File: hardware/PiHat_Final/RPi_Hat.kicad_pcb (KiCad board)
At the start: 2 copper layers, 65 x 56.5 mm, 5 parts, among them J2 RPi_GPIO

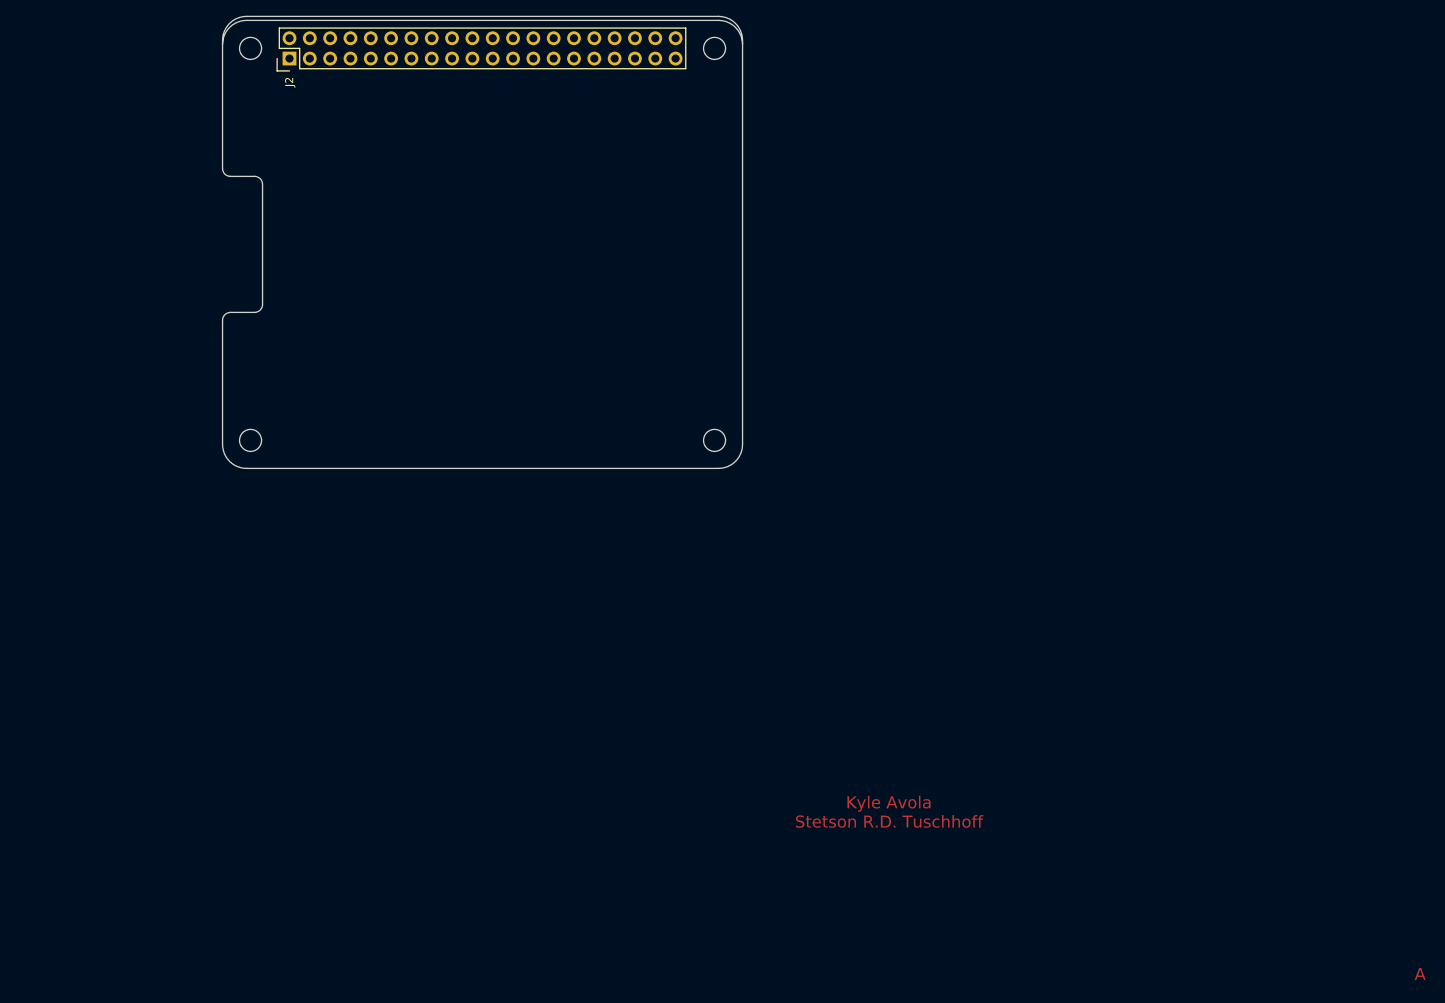
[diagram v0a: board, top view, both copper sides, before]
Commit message: Began Layout, Pihat final.
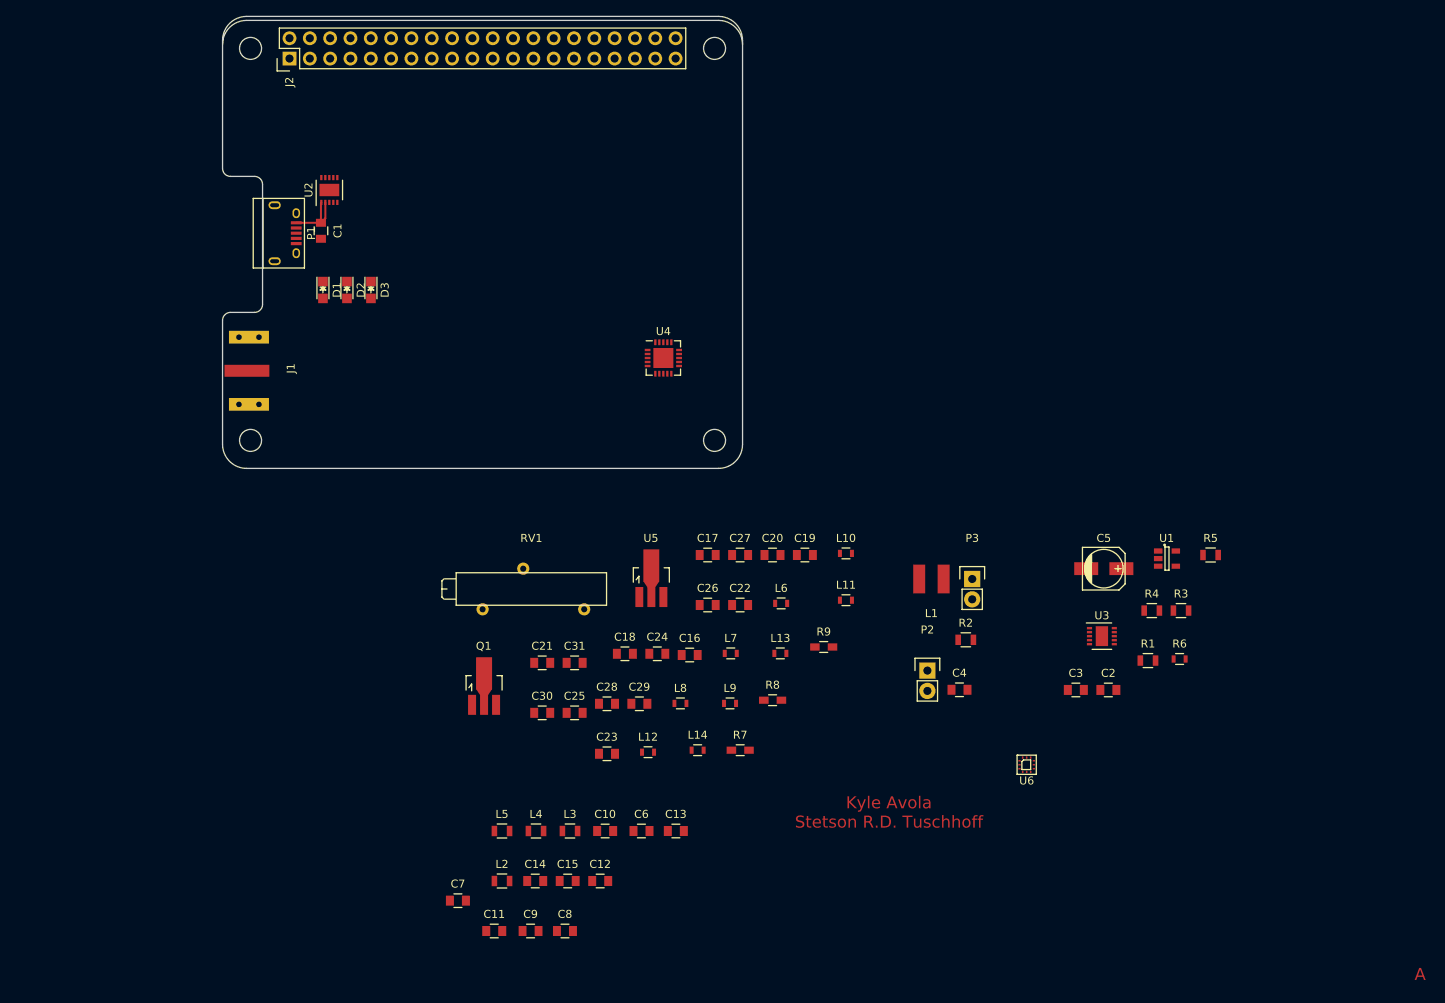
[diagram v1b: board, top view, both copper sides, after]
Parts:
- added C1: 10uF, Capacitors_SMD:C_0805, F.Cu at (131.2, 100.1)
- added C10: 5.6pF, Capacitors_SMD:C_0805, F.Cu at (166.8, 175.1)
- added C11: 4.7pF, Capacitors_SMD:C_0805, F.Cu at (152.9, 187.6)
- added C12: 10nF, Capacitors_SMD:C_0805, F.Cu at (166.2, 181.4)
- added C13: 10nF, Capacitors_SMD:C_0805, F.Cu at (175.6, 175.1)
- added C14: 20pF, Capacitors_SMD:C_0805, F.Cu at (158.0, 181.4)
- added C15: 20pF, Capacitors_SMD:C_0805, F.Cu at (162.1, 181.4)
- added C16: C, Capacitors_SMD:C_0805, F.Cu at (177.3, 153.1)
- added C17: C, Capacitors_SMD:C_0805, F.Cu at (179.6, 140.6)
- added C18: C, Capacitors_SMD:C_0805, F.Cu at (169.2, 153.0)
- added C19: C, Capacitors_SMD:C_0805, F.Cu at (191.7, 140.6)
- added C2: 10uF, Capacitors_SMD:C_0805, F.Cu at (229.7, 157.5)
- added C20: C, Capacitors_SMD:C_0805, F.Cu at (187.7, 140.6)
- added C21: C, Capacitors_SMD:C_0805, F.Cu at (158.9, 154.1)
- added C22: C, Capacitors_SMD:C_0805, F.Cu at (183.6, 146.9)
- added C23: C, Capacitors_SMD:C_0805, F.Cu at (167.0, 165.5)
- added C24: C, Capacitors_SMD:C_0805, F.Cu at (173.3, 153.0)
- added C25: C, Capacitors_SMD:C_0805, F.Cu at (163.0, 160.4)
- added C26: C, Capacitors_SMD:C_0805, F.Cu at (179.6, 146.9)
- added C27: C, Capacitors_SMD:C_0805, F.Cu at (183.6, 140.6)
- added C28: C, Capacitors_SMD:C_0805, F.Cu at (167.0, 159.2)
- added C29: C, Capacitors_SMD:C_0805, F.Cu at (171.1, 159.2)
- added C3: 10uF, Capacitors_SMD:C_0805, F.Cu at (225.6, 157.5)
- added C30: C, Capacitors_SMD:C_0805, F.Cu at (158.9, 160.4)
- added C31: C, Capacitors_SMD:C_0805, F.Cu at (163.0, 154.1)
- added C4: 10uF, Capacitors_SMD:C_0805, F.Cu at (211.1, 157.5)
- added C5: 47uF, Capacitors_SMD:c_elec_5x5.3, F.Cu at (229.1, 142.3)
- added C6: 4.7pF, Capacitors_SMD:C_0805, F.Cu at (171.3, 175.1)
- added C7: 5.1pF, Capacitors_SMD:C_0805, F.Cu at (148.4, 183.8)
- added C8: 12pF, Capacitors_SMD:C_0805, F.Cu at (161.8, 187.6)
- added C9: 4.7pF, Capacitors_SMD:C_0805, F.Cu at (157.5, 187.6)
- added D1: LED, LEDs:LED_0805, F.Cu at (131.5, 107.5)
- added D2: LED, LEDs:LED_0805, F.Cu at (134.5, 107.5)
- added D3: LED, LEDs:LED_0805, F.Cu at (137.5, 107.5)
- added J1: SMACONN, RF BW Filter:SMA_Edge_Mount, F.Cu at (122.0, 117.6)
- added L1: 6.8uH, inductor:BOURNES_SRN4018, F.Cu at (207.6, 143.6)
- added L10: L_Small, Resistors_SMD:R_0603, F.Cu at (196.9, 140.4)
- added L11: L_Small, Resistors_SMD:R_0603, F.Cu at (196.9, 146.3)
- added L12: L_Small, Resistors_SMD:R_0603, F.Cu at (172.1, 165.3)
- added L13: L_Small, Resistors_SMD:R_0603, F.Cu at (188.7, 152.9)
- added L14: L_Small, Resistors_SMD:R_0603, F.Cu at (178.3, 165.0)
- added L2: 11nH, Resistors_SMD:R_0805, F.Cu at (153.9, 181.4)
- added L3: 27nH, Resistors_SMD:R_0805, F.Cu at (162.4, 175.1)
- added L4: 36nH, Resistors_SMD:R_0805, F.Cu at (158.1, 175.1)
- added L5: 36nH, Resistors_SMD:R_0805, F.Cu at (153.9, 175.1)
- added L6: L_Small, Resistors_SMD:R_0603, F.Cu at (188.8, 146.7)
- added L7: L_Small, Resistors_SMD:R_0603, F.Cu at (182.5, 152.9)
- added L8: L_Small, Resistors_SMD:R_0603, F.Cu at (176.2, 159.2)
- added L9: L_Small, Resistors_SMD:R_0603, F.Cu at (182.4, 159.2)
- added P1: USB_OTG, Connect:USB_Micro-B, F.Cu at (126.6, 100.4)
- added P2: BATT, Pin_Headers:Pin_Header_Straight_1x02, F.Cu at (207.1, 155.1)
- added P3: THERM, Pin_Headers:Pin_Header_Straight_1x02, F.Cu at (212.7, 143.6)
- added Q1: AFT05MS003N, TO_SOT_Packages_SMD:SOT89-3_Housing_Handsoldering, F.Cu at (151.6, 157.0)
- added R1: 1K, Resistors_SMD:R_0805, F.Cu at (234.6, 153.8)
- added R2: 1K, Resistors_SMD:R_0805, F.Cu at (211.9, 151.2)
- added R3: 1K, Resistors_SMD:R_0805, F.Cu at (238.8, 147.6)
- added R4: 1K, Resistors_SMD:R_0805, F.Cu at (235.1, 147.6)
- added R5: 1K, Resistors_SMD:R_0805, F.Cu at (242.5, 140.6)
- added R6: 150K, Resistors_SMD:R_0603, F.Cu at (238.6, 153.6)
- added R7: R, Resistors_SMD:R_0603_HandSoldering, F.Cu at (183.7, 165.0)
- added R8: R, Resistors_SMD:R_0603_HandSoldering, F.Cu at (187.7, 158.8)
- added R9: R, Resistors_SMD:R_0603_HandSoldering, F.Cu at (194.1, 152.1)
- added RV1: POT, Potentiometers:Potentiometer_Bourns_3006W_Angular_ScrewFront, F.Cu at (164.2, 147.4)
- added U1: MCP3021, TO_SOT_Packages_SMD:SOT-23-5, F.Cu at (237.0, 141.1)
- added U2: MCP73833, Housings_DFN_QFN:DFN-10-1EP_3x3mm_Pitch0.5mm, F.Cu at (132.3, 95.0)
- added U3: TPS61027, Housings_DFN_QFN:DFN-10-1EP_3x3mm_Pitch0.5mm, F.Cu at (228.9, 150.8)
- added U4: Si4464, Housings_DFN_QFN:QFN-20-1EP_4x4mm_Pitch0.5mm, F.Cu at (174.1, 116.0)
- added U5: MMG3H21NT1, TO_SOT_Packages_SMD:SOT89-3_Housing_Handsoldering, F.Cu at (172.5, 143.5)
- added U6: SKY13374, RFBRD:QFN_12_2mmx2mm_0.5PITCH, F.Cu at (219.5, 166.8)
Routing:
- net 5VU: track 0.00 -> 8.44 mm

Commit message: PCB Layout Changes
minor changes, will continue layout
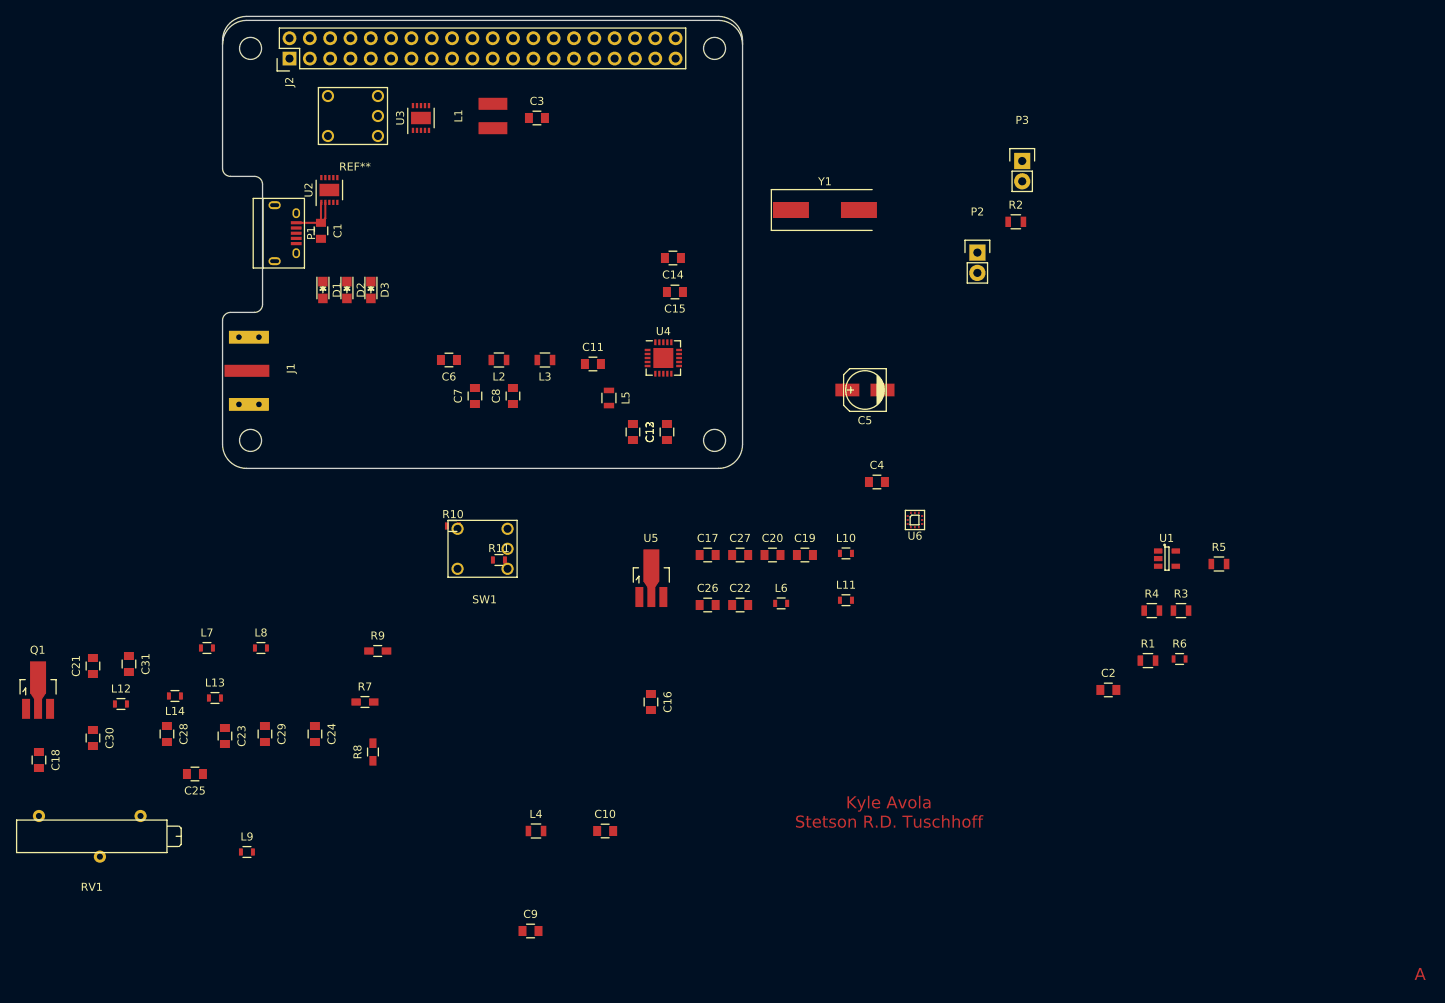
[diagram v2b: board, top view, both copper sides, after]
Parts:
- added R10: R, Resistors_SMD:R_0603, F.Cu at (147.8, 137.0)
- added R11: R, Resistors_SMD:R_0603, F.Cu at (153.5, 141.2)
- added REF**: rotary_potentiometer, rotary_potentiometer:rotary_potentiometer, F.Cu at (135.2, 85.8)
- added SW1: PWR_VOL, rotary_potentiometer:rotary_potentiometer, F.Cu at (151.4, 139.9)
- added Y1: 30MHz, Crystals:Crystal_SMD_HC49-SD, F.Cu at (194.2, 97.5)
- moved U3 107.0 mm to (143.8, 86.0), turned to 90 degrees
- moved C3 98.2 mm to (158.2, 86.0)
- moved C14 79.8 mm to (175.2, 103.5), turned to 180 degrees
- moved L1 79.7 mm to (152.8, 85.8), turned to 270 degrees
- moved C15 74.8 mm to (175.5, 107.8), turned to 180 degrees
- moved C18 74.4 mm to (96.0, 166.2), turned to 270 degrees
- moved RV1 72.9 mm to (96.0, 173.2), turned to 180 degrees
- moved C11 71.9 mm to (165.2, 116.8)
- moved L13 70.9 mm to (118.0, 158.5)
- moved C8 67.2 mm to (155.2, 120.8), turned to 90 degrees
- moved L12 66.2 mm to (106.2, 159.2)
- moved L14 65.7 mm to (113.0, 158.2), turned to 180 degrees
- moved L7 65.5 mm to (117.0, 152.2)
- moved L2 65.1 mm to (153.5, 116.2), turned to 180 degrees
- moved C6 63.6 mm to (147.2, 116.2), turned to 180 degrees
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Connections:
- J2 pad 1: (no net) -> Net-(J2-Pad1)
- J2 pad 10: (no net) -> Net-(J2-Pad10)
- J2 pad 11: (no net) -> Net-(J2-Pad11)
- J2 pad 12: (no net) -> Net-(J2-Pad12)
- J2 pad 13: (no net) -> Net-(J2-Pad13)
- J2 pad 14: (no net) -> Net-(J2-Pad14)
- J2 pad 15: (no net) -> Net-(J2-Pad15)
- J2 pad 16: (no net) -> Net-(J2-Pad16)
- J2 pad 17: (no net) -> Net-(J2-Pad17)
- J2 pad 18: (no net) -> Net-(J2-Pad18)
- J2 pad 19: (no net) -> Net-(J2-Pad19)
- J2 pad 2: (no net) -> Net-(J2-Pad2)
- J2 pad 20: (no net) -> Net-(J2-Pad20)
- J2 pad 21: (no net) -> Net-(J2-Pad21)
- J2 pad 22: (no net) -> Net-(J2-Pad22)
- J2 pad 23: (no net) -> Net-(J2-Pad23)
- J2 pad 24: (no net) -> Net-(J2-Pad24)
- J2 pad 25: (no net) -> Net-(J2-Pad25)
- J2 pad 26: (no net) -> Net-(J2-Pad26)
- J2 pad 27: (no net) -> Net-(J2-Pad27)
- J2 pad 28: (no net) -> Net-(J2-Pad28)
- J2 pad 29: (no net) -> Net-(J2-Pad29)
- J2 pad 3: (no net) -> Net-(J2-Pad3)
- J2 pad 30: (no net) -> Net-(J2-Pad30)
- J2 pad 31: (no net) -> Net-(J2-Pad31)
- J2 pad 32: (no net) -> Net-(J2-Pad32)
- J2 pad 33: (no net) -> Net-(J2-Pad33)
- J2 pad 34: (no net) -> Net-(J2-Pad34)
- J2 pad 35: (no net) -> Net-(J2-Pad35)
- J2 pad 36: (no net) -> Net-(J2-Pad36)
- J2 pad 37: (no net) -> Net-(J2-Pad37)
- J2 pad 38: (no net) -> Net-(J2-Pad38)
- J2 pad 39: (no net) -> Net-(J2-Pad39)
- J2 pad 4: (no net) -> Net-(J2-Pad4)
- J2 pad 40: (no net) -> Net-(J2-Pad40)
- J2 pad 5: (no net) -> Net-(J2-Pad5)
- J2 pad 6: (no net) -> Net-(J2-Pad6)
- J2 pad 7: (no net) -> Net-(J2-Pad7)
- J2 pad 8: (no net) -> Net-(J2-Pad8)
- J2 pad 9: (no net) -> Net-(J2-Pad9)
- P1 pad 2: (no net) -> Net-(P1-Pad2)
- P1 pad 3: (no net) -> Net-(P1-Pad3)
- P1 pad 4: (no net) -> Net-(P1-Pad4)
- U1 pad 3: (no net) -> VOL
- U1 pad 4: (no net) -> SDA
- U1 pad 5: (no net) -> SCL
- U3 pad 3: (no net) -> Net-(U3-Pad3)
- U3 pad 4: (no net) -> Net-(U3-Pad4)
- U3 pad 7: (no net) -> Net-(U3-Pad7)
- U4 pad 1: (no net) -> SHDN
- U4 pad 10: (no net) -> Net-(U4-Pad10)
- U4 pad 11: (no net) -> nIRQ
- U4 pad 12: (no net) -> SCLK
- U4 pad 13: (no net) -> SDO
- U4 pad 14: (no net) -> SDI
- U4 pad 15: (no net) -> nSEL
- U4 pad 19: (no net) -> Net-(U4-Pad19)
- U4 pad 20: (no net) -> Net-(U4-Pad20)
- U4 pad 5: (no net) -> Net-(U4-Pad5)
- U4 pad 7: (no net) -> Net-(U4-Pad7)
- U4 pad 9: (no net) -> Net-(U4-Pad9)
- U6 pad 1: (no net) -> Net-(U6-Pad1)
- U6 pad 7: (no net) -> SEL_1

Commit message: Pihat PCB Changes
layout
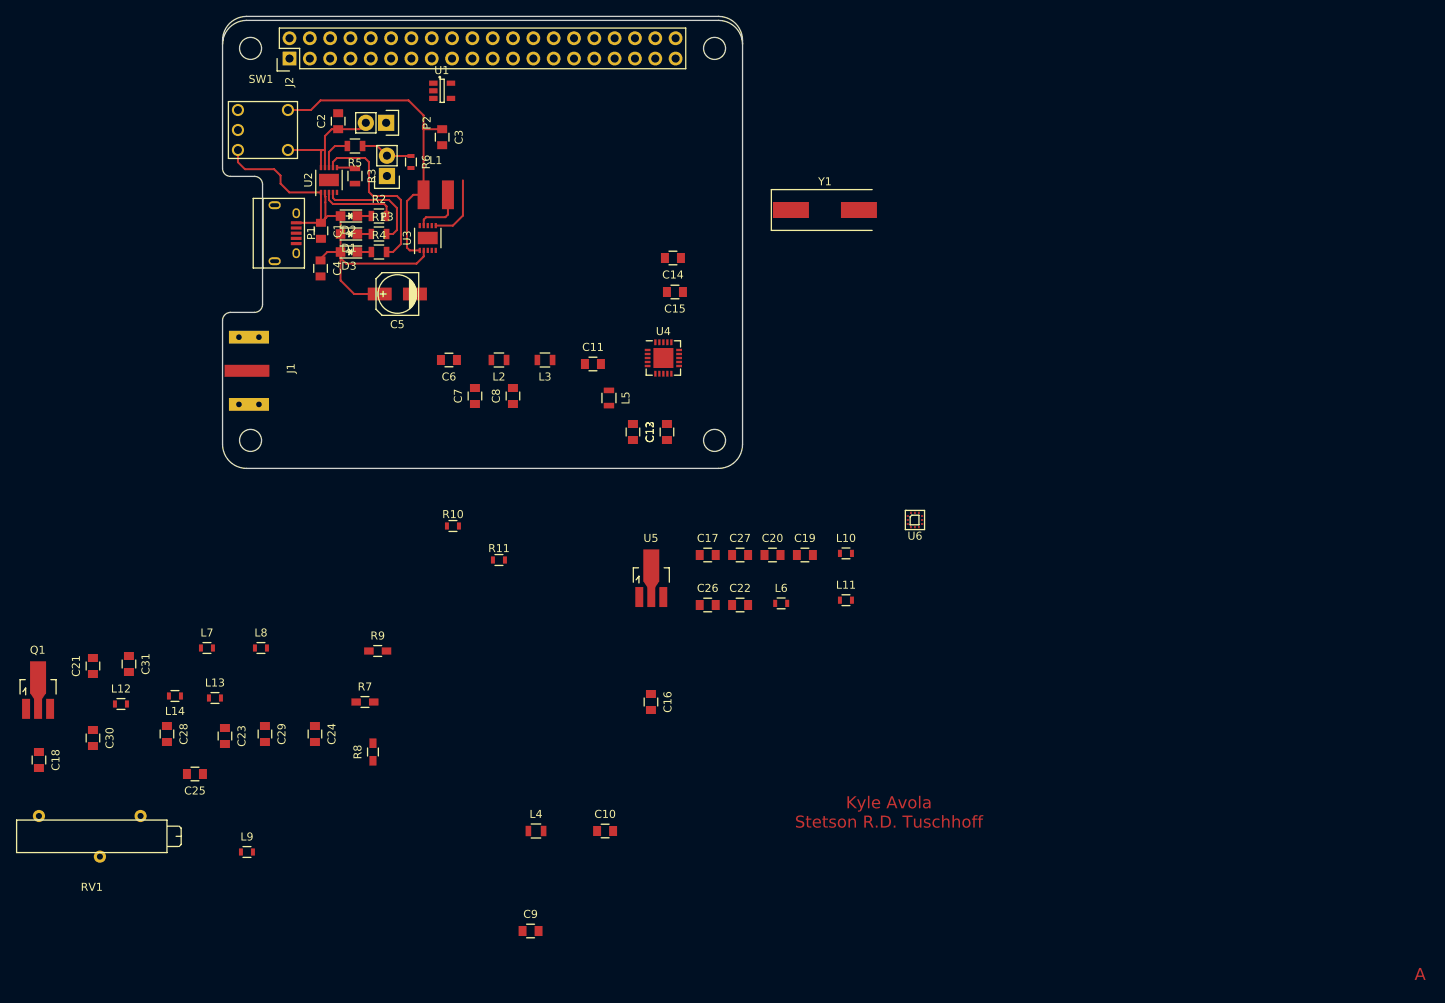
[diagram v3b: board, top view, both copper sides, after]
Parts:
- removed REF**: rotary_potentiometer, rotary_potentiometer:rotary_potentiometer
- moved R5 120.0 mm to (135.5, 89.5), turned to 180 degrees
- moved C2 119.7 mm to (133.4, 86.4), turned to 90 degrees
- moved R3 116.7 mm to (135.5, 93.2), turned to 270 degrees
- moved R6 114.4 mm to (142.5, 91.5), turned to 270 degrees
- moved R1 109.9 mm to (138.5, 100.5)
- moved U1 107.8 mm to (146.4, 82.6)
- moved R4 106.5 mm to (138.5, 102.8)
- moved R2 79.6 mm to (138.5, 98.2)
- moved P3 79.4 mm to (139.5, 93.2), turned to 180 degrees
- moved P2 75.7 mm to (139.4, 86.6), turned to 270 degrees
- moved C4 74.5 mm to (131.2, 104.8), turned to 270 degrees
- moved C5 59.7 mm to (140.8, 108.0)
- moved SW1 59.1 mm to (124.0, 87.5), turned to 180 degrees
- moved U3 15.0 mm to (144.6, 101.0)
- moved L1 12.2 mm to (145.6, 95.6), turned to 180 degrees
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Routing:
- net VBAT: track 0.00 -> 49.2 mm
- net 5VU: track 8.44 -> 57.1 mm
- net Net-(R4-Pad2): track 0.00 -> 21.5 mm
- net VBP_SW: track 0.00 -> 16.6 mm
- net Net-(R1-Pad2): track 0.00 -> 13.5 mm
- net Net-(R2-Pad2): track 0.00 -> 9.68 mm
- net Net-(P3-Pad2): track 0.00 -> 6.57 mm
- net Net-(L1-Pad1): track 0.00 -> 6.51 mm
- net Net-(R5-Pad2): track 0.00 -> 4.56 mm
- net Net-(R3-Pad1): track 0.00 -> 2.29 mm
- net Net-(D3-Pad1): track 0.00 -> 1.75 mm
- net Net-(D2-Pad1): track 0.00 -> 1.75 mm
- net Net-(D1-Pad1): track 0.00 -> 1.75 mm

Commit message: Pihat Update Again
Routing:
- net (no net): track 0.00 -> 6.96 mm
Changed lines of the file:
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@@
     (links 144)
     (no_connects 118)
-    (area 118.899999 73.249999 184.000001 129.850001)
+    (area 90.35 72.3245 269.292857 194.4)
     (thickness 1.6)
     (drawings 25)
-    (tracks 101)
+    (tracks 104)
     (zones 0)
     (modules 78)
@@
   (gr_line (start 183.95 76.3) (end 183.95 126.8) (angle 90) (layer Edge.Cuts) (width 0.1))
   (gr_line (start 121.95 73.3) (end 180.95 73.3) (angle 90) (layer Edge.Cuts) (width 0.1))
+  (segment (start 151.5 83.25) (end 157.5 83.25) (width 0.25) (layer F.Cu) (net 0))
+  (segment (start 158 83.75) (end 158.25 83.75) (width 0.25) (layer F.Cu) (net 0))
+  (segment (start 157.5 83.25) (end 158 83.75) (width 0.25) (layer F.Cu) (net 0))
   (segment (start 120.875 90) (end 120.875 91.525) (width 0.25) (layer F.Cu) (net 1))
   (segment (start 127.3 95.3) (end 131.25 95.3) (width 0.25) (layer F.Cu) (net 1))
